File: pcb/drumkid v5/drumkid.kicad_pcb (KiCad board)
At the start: 2 copper layers, 51 parts, among them J1 Conn_01x02_Female, J5 Conn_01x05_Female, J6 Conn_01x04_Female, J7 Conn_01x06_Female, J8 Conn_01x05_Female, J9 AudioJack3_Ground_Switch, SW1 SW_SPDT, SW2 SW_Push, SW3 SW_Push, SW4 SW_Push, SW5 SW_Push, SW6 SW_Push, SW7 SW_Push, U2 ATmega328P-PU, U3 LM386, Y1 Crystal

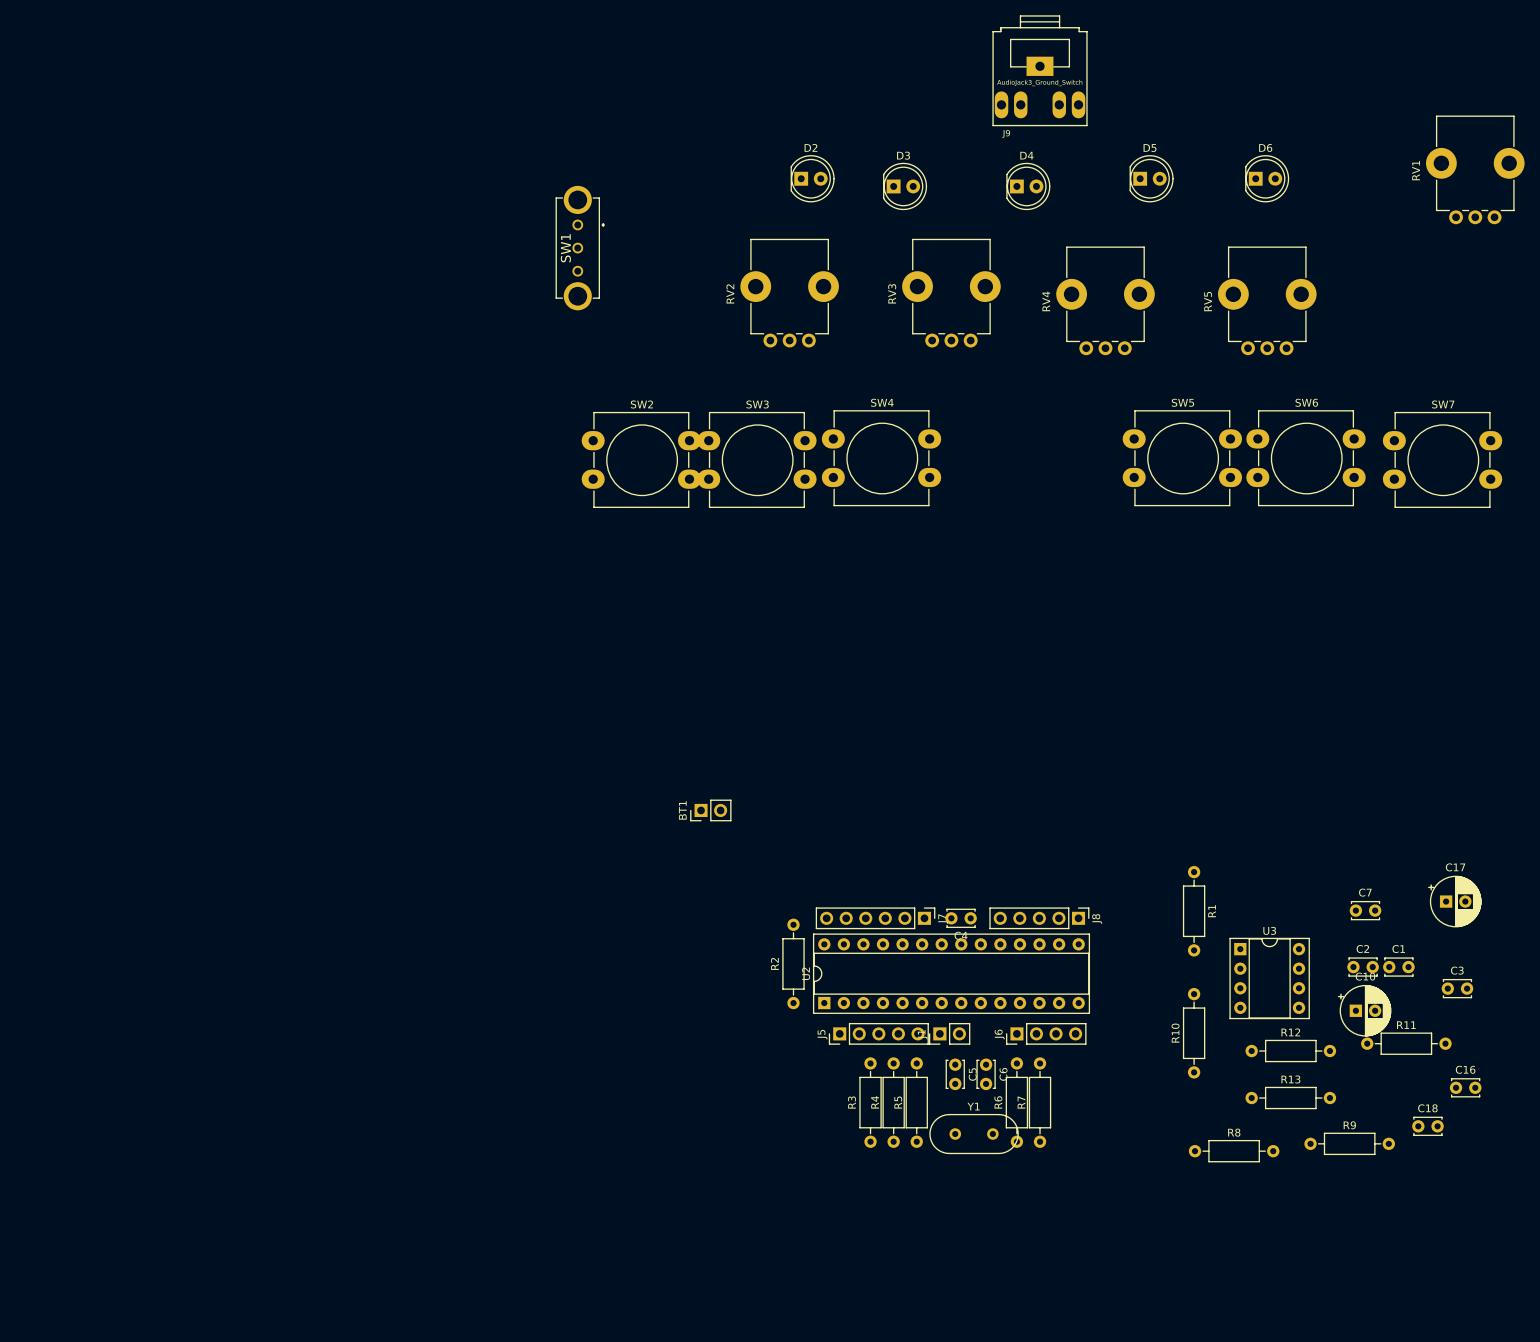
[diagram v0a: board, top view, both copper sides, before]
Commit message: lots of new stuff - pcb v5 progress, midi code progress, but lots to be done
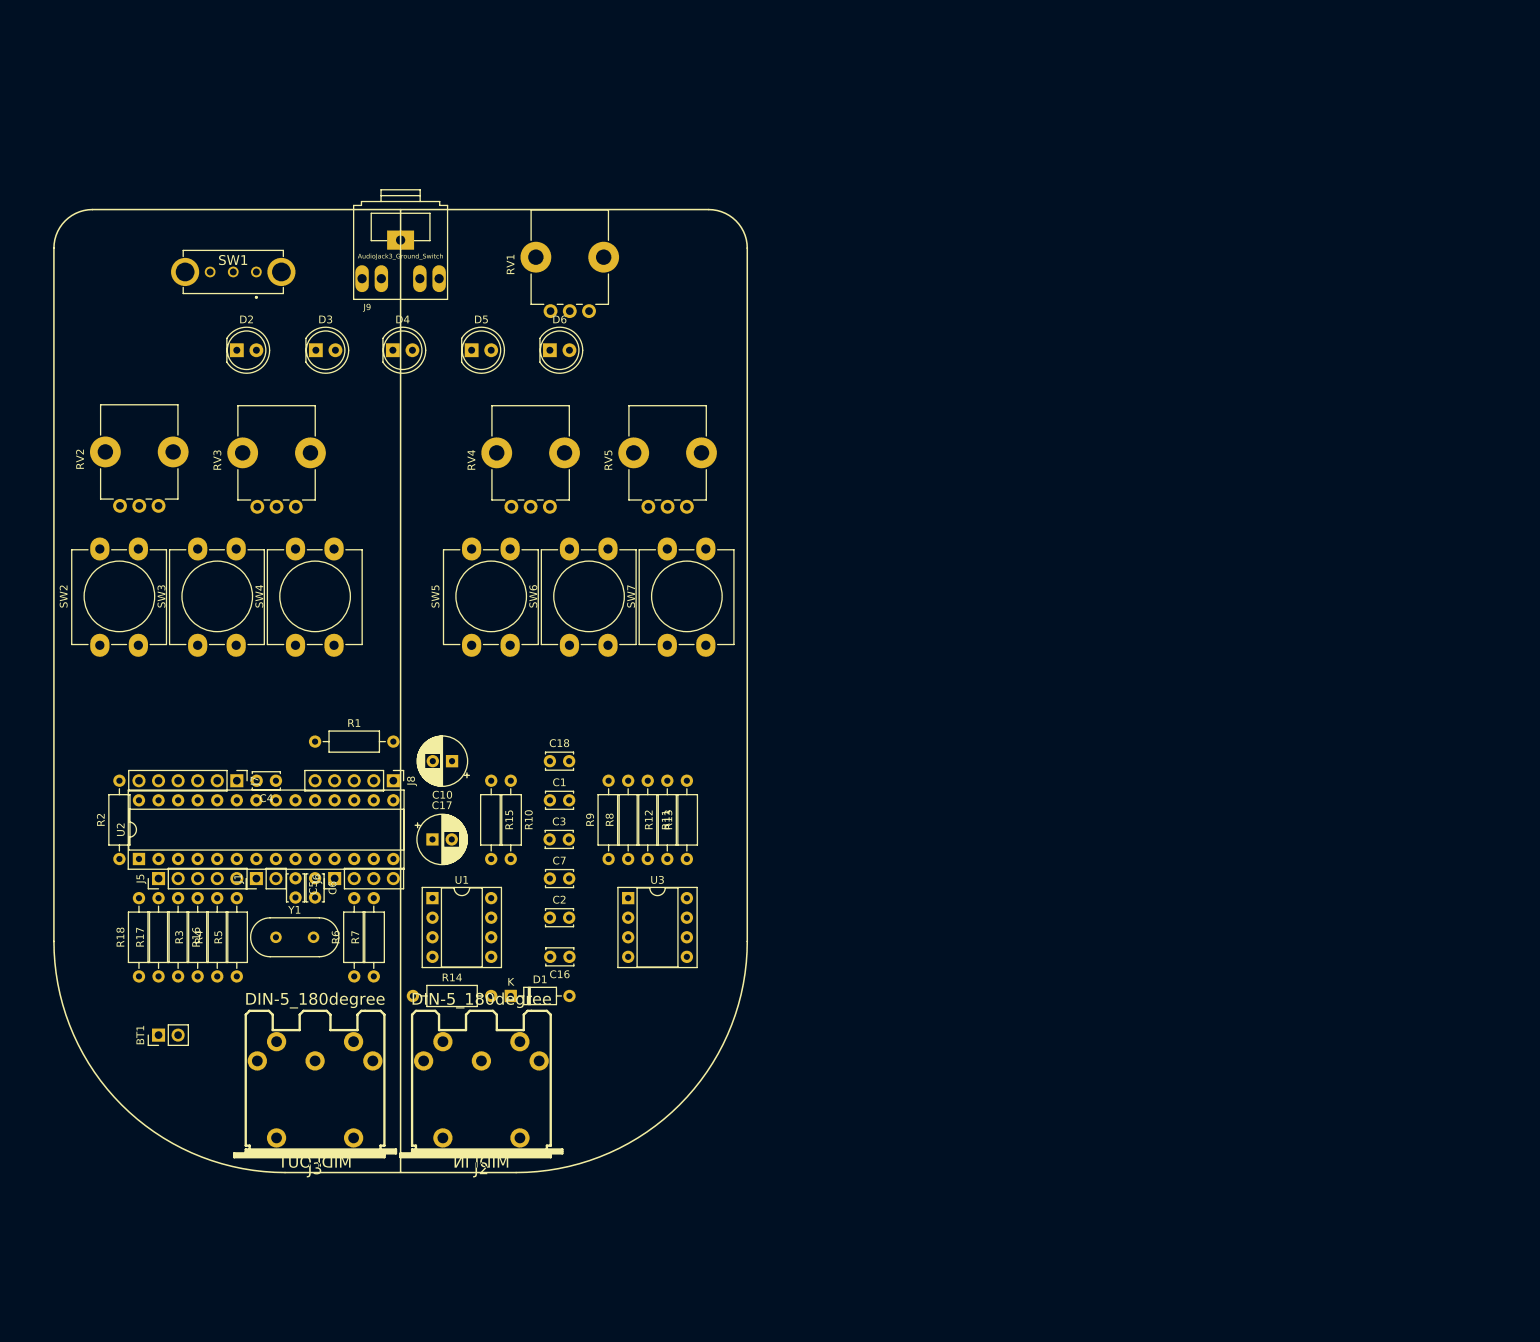
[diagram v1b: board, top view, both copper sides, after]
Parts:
- added D1: 1N4148, Diode_THT:D_DO-35_SOD27_P7.62mm_Horizontal, F.Cu at (114.3, 132.1)
- added J2: DIN-5_180degree, Eurocad:MIDI_DIN5, F.Cu at (110.5, 143.5)
- added J3: DIN-5_180degree, Eurocad:MIDI_DIN5, F.Cu at (88.9, 143.5)
- added R14: 220, Resistor_THT:R_Axial_DIN0207_L6.3mm_D2.5mm_P10.16mm_Horizontal, F.Cu at (101.6, 132.1)
- added R15: 10k, Resistor_THT:R_Axial_DIN0207_L6.3mm_D2.5mm_P10.16mm_Horizontal, F.Cu at (111.8, 104.1)
- added R16: 220, Resistor_THT:R_Axial_DIN0207_L6.3mm_D2.5mm_P10.16mm_Horizontal, F.Cu at (71.1, 119.4)
- added R17: 470, Resistor_THT:R_Axial_DIN0207_L6.3mm_D2.5mm_P10.16mm_Horizontal, F.Cu at (68.6, 129.5)
- added R18: 220, Resistor_THT:R_Axial_DIN0207_L6.3mm_D2.5mm_P10.16mm_Horizontal, F.Cu at (66.0, 129.5)
- added U1: 6N138, Package_DIP:DIP-8_W7.62mm_Socket, F.Cu at (104.1, 119.4)
- moved C17 131.8 mm to (104.1, 111.8)
- moved C18 122.3 mm to (119.4, 101.6)
- moved C10 121.7 mm to (106.7, 101.6), turned to 180 degrees
- moved C3 118.2 mm to (119.3, 111.8)
- moved RV1 118.2 mm to (124.5, 43.2)
- moved C16 116.3 mm to (121.9, 127.0), turned to 180 degrees
- moved R1 115.4 mm to (88.9, 99.1), turned to 0 degrees
- moved C1 111.1 mm to (119.4, 106.7)
- moved C7 104.7 mm to (119.4, 116.8)
- moved C2 104.5 mm to (119.4, 121.9)
- moved R11 99.4 mm to (132.1, 104.1), turned to 270 degrees
- moved R9 98.3 mm to (127.0, 114.3), turned to 90 degrees
- moved SW7 98.0 mm to (134.6, 86.6), turned to 90 degrees
- moved R10 96.4 mm to (114.3, 104.1), turned to 270 degrees
- moved D6 94.3 mm to (119.4, 48.3)
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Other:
- board text added: "MIDI IN"
- board text added: "MIDI OUT"

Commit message: more pcb progress
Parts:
- added D7: LED, LED_THT:LED_D5.0mm, B.Cu at (69.0, 50.0)
- added R19: 220, Resistor_THT:R_Axial_DIN0207_L6.3mm_D2.5mm_P10.16mm_Horizontal, F.Cu at (61.0, 104.1)
- BT1: footprint Connector_PinHeader_2.54mm:PinHeader_1x02_P2.54mm_Vertical -> Connector_Wire:SolderWirePad_1x02_P5.08mm_Drill1.5mm
- D2, D3, D4, D5, D6, J9, RV1, RV2, RV3, RV4, RV5, SW1, SW2, SW3, SW4, SW5, SW6, SW7: moved to B.Cu
- moved BT1 38.2 mm to (66.0, 99.1), turned to 0 degrees
- moved R14 33.1 mm to (134.6, 129.5), turned to 180 degrees
- moved R7 20.5 mm to (116.8, 127.0), turned to 180 degrees
- moved D1 13.7 mm to (127.0, 127.0)
- moved R6 10.5 mm to (104.1, 127.0), turned to 180 degrees
- moved D4 10.2 mm to (109.0, 50.0)
- moved D5 9.93 mm to (119.0, 50.0)
- moved D6 9.78 mm to (129.0, 50.0)
- moved SW2 7.82 mm to (61.0, 78.7), turned to 270 degrees
- moved SW3 7.82 mm to (73.7, 78.7), turned to 270 degrees
- moved SW4 7.82 mm to (86.4, 78.7), turned to 270 degrees
- moved SW5 7.82 mm to (109.2, 78.7), turned to 270 degrees
- moved SW6 7.82 mm to (121.9, 78.7), turned to 270 degrees
- moved SW7 7.82 mm to (134.6, 78.7), turned to 270 degrees
- moved RV3 5.12 mm to (81.3, 68.6)
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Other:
- board text added: "chance/pitch slop/beat drop"
- board text added: "midpoint/glitch delay_mix/drift drone pitch"
- board text added: "off"
- board text added: "on"
- board text added: "range/crop delay/time_sig drone mix"
- board text added: "zoom/crush swing/tempo drone_mod"

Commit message: more pcb stuff
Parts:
- added H1: MountingHole, MountingHole:MountingHole_3.2mm_M3, F.Cu at (60.0, 35.0)
- added H2: MountingHole, MountingHole:MountingHole_3.2mm_M3, F.Cu at (60.0, 110.0)
- added H3: MountingHole, MountingHole:MountingHole_3.2mm_M3, F.Cu at (70.0, 160.0)
- added H4: MountingHole, MountingHole:MountingHole_3.2mm_M3, F.Cu at (130.0, 160.0)
- added H5: MountingHole, MountingHole:MountingHole_3.2mm_M3, F.Cu at (140.0, 110.0)
- added H6: MountingHole, MountingHole:MountingHole_3.2mm_M3, F.Cu at (140.0, 35.0)
- moved R10 33.0 mm to (114.3, 132.1)
- moved R15 33.0 mm to (111.8, 132.1)
- moved R7 27.5 mm to (94.0, 142.2), turned to 90 degrees
- moved U1 20.9 mm to (99.1, 134.6)
- moved R6 19.8 mm to (91.4, 142.2), turned to 90 degrees
- moved J2 17.8 mm to (111.8, 157.5)
- moved J3 17.8 mm to (88.9, 157.5)
- moved C17 16.1 mm to (111.8, 124.5)
- moved Y1 15.2 mm to (83.8, 139.7), turned to 90 degrees
- moved C10 13.7 mm to (111.8, 114.3)
- moved R16 13.0 mm to (71.1, 132.1)
- moved R18 13.0 mm to (66.0, 142.2)
- moved R4 13.0 mm to (76.2, 142.2)
- moved R17 13.0 mm to (68.6, 142.2)
- moved R3 13.0 mm to (73.7, 142.2)
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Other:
- board text added: "A"
- board text added: "B"
- board text added: "C"
- board text added: "SERIAL NUMBER"
- board text added: "X"
- board text added: "Y"
- board text added: "Z"
- board text removed: "chance/pitch slop/beat drop"
- board text removed: "midpoint/glitch delay_mix/drift drone pitch"
- board text removed: "range/crop delay/time_sig drone mix"
- board text removed: "zoom/crush swing/tempo drone_mod"

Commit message: and more pcb stuff
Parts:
- added H7: MountingHole, MountingHole:MountingHole_3.2mm_M3, F.Cu at (100.0, 50.0)
- added H8: MountingHole, MountingHole:MountingHole_3.2mm_M3, F.Cu at (100.0, 80.0)
- moved RV1 12.0 mm to (115.0, 44.0)
- moved R1 8.03 mm to (81.3, 106.7)
- moved SW1 3.38 mm to (79.0, 40.0)
- moved RV3 2.54 mm to (78.7, 68.6)
- moved RV4 2.54 mm to (116.8, 68.6)
- moved BT1 2.54 mm to (71.1, 106.7)
- moved J9 1.44 mm to (100.0, 37.0)
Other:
- board outline added: 90 x 140 mm
- board text added: "0"
- board text added: "1"
- board text added: "8 7 6 5 GND VCC 4 3 2 1 0"
- board text added: "9 10 11 12 13 A0 A1 A2 A3 A4 A5"
- board text added: "d"
- board text added: "k"
- board text removed: "off"
- board text removed: "on"

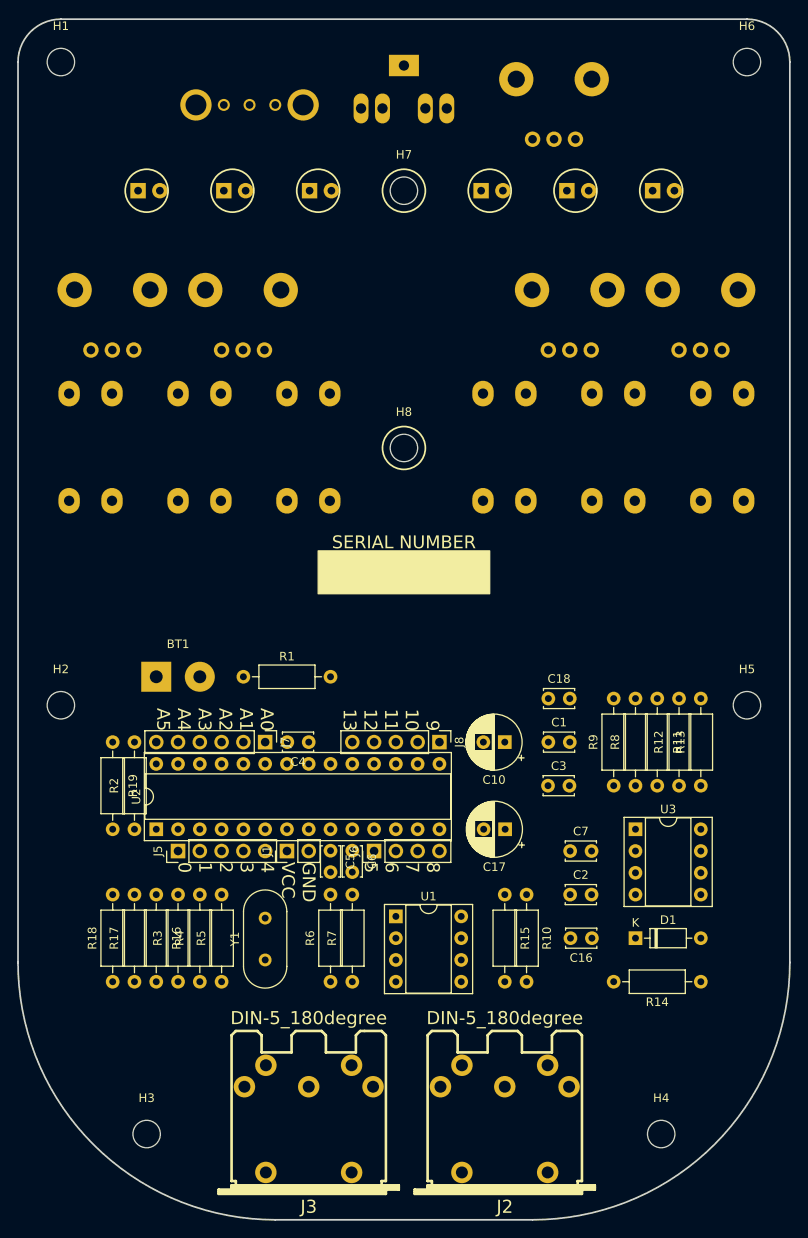
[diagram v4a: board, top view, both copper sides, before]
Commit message: finished messing about with pcb layout, next comes routing...
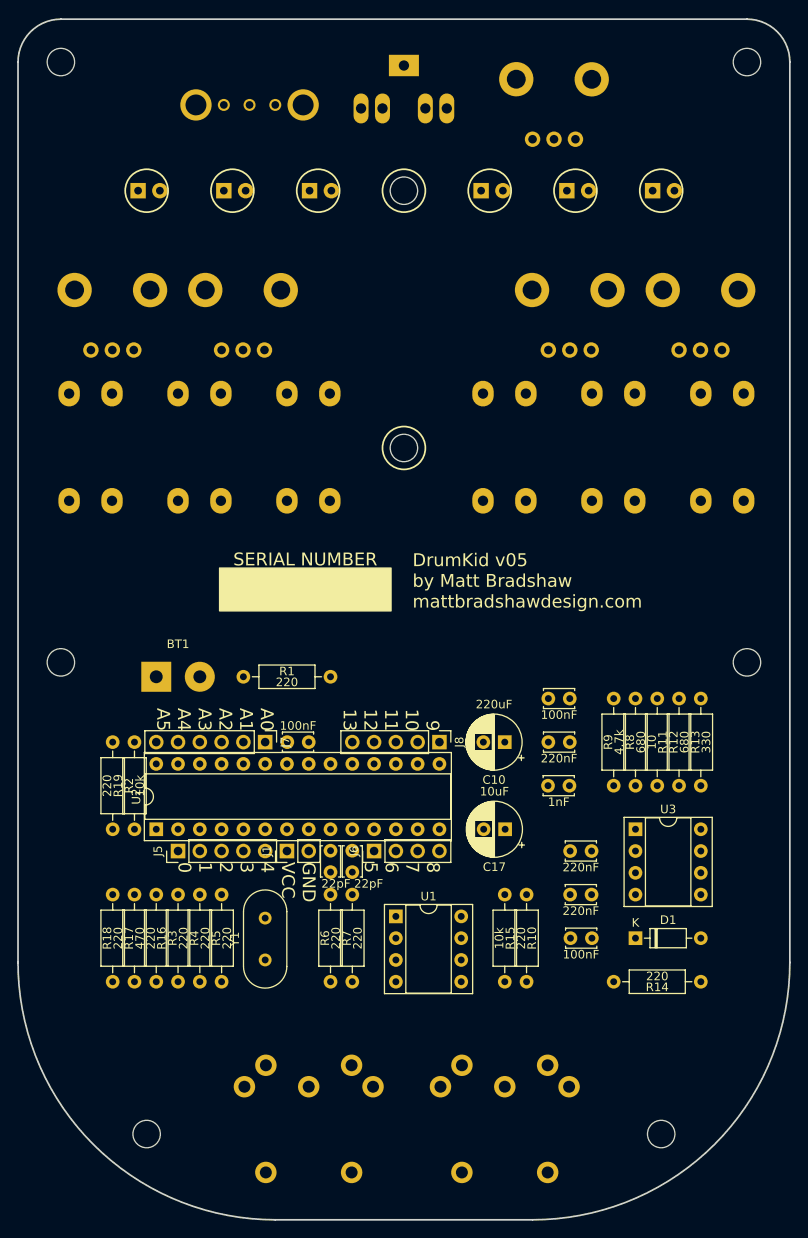
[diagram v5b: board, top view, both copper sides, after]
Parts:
- C1, C16, C18, C2, C3, C4, C5, C6, C7: footprint Capacitor_THT:C_Disc_D3.4mm_W2.1mm_P2.50mm -> drumkidcustom:C_Disc_D3.4mm_W2.1mm_P2.50mm
- C10, C17: footprint Capacitor_THT:CP_Radial_D6.3mm_P2.50mm -> drumkidcustom:CP_Radial_D6.3mm_P2.50mm
- D2, D3, D4, D5, D6, D7: footprint LED_THT:LED_D5.0mm -> drumkidcustom:LED_D5.0mm
- H1, H2, H3, H4, H5, H6, H7, H8: footprint MountingHole:MountingHole_3.2mm_M3 -> drumkidcustom:MountingHole_3.2mm_M3
- J2, J3: footprint Eurocad:MIDI_DIN5 -> drumkidcustom:MIDI_DIN5
- J9: footprint headphone:Tayda_3.5mm_stereo_TRS_jack_A-853 -> drumkidcustom:Tayda_3.5mm_stereo_TRS_jack_A-853
- R1, R10, R11, R12, R13, R14, R15, R16, R17, R18, R19, R2, R3, R4, R5, R6, R7, R8, R9: footprint Resistor_THT:R_Axial_DIN0207_L6.3mm_D2.5mm_P10.16mm_Horizontal -> drumkidcustom:R_Axial_DIN0207_L6.3mm_D2.5mm_P10.16mm_Horizontal
- SW1: footprint SamacSys_Parts:EG1206 -> drumkidcustom:EG1206
- SW2, SW3, SW4, SW5, SW6, SW7: footprint Button_Switch_THT:SW_PUSH-12mm_Wuerth-430476085716 -> drumkidcustom:SW_PUSH-12mm_Wuerth-430476085716
- moved H2 5.00 mm to (60.0, 105.0)
- moved H5 5.00 mm to (140.0, 105.0)
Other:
- board text added: "DrumKid v05 by Matt Bradshaw mattbradshawdesign.com"

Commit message: routing done except for gnd
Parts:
- moved RV2 68.6 mm to (132.1, 68.6)
- moved RV5 68.6 mm to (63.5, 68.6)
- moved RV3 38.1 mm to (116.8, 68.6)
- moved RV4 38.1 mm to (78.7, 68.6)
- moved Y1 5.24 mm to (85.1, 134.6), turned to 270 degrees
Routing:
- net +5V: track 0.00 -> 295.7 mm
- net Net-(D4-Pad2): track 0.00 -> 184.2 mm
- net Net-(D5-Pad2): track 0.00 -> 162.1 mm
- net Net-(D3-Pad2): track 0.00 -> 139.0 mm
- net Net-(D6-Pad2): track 0.00 -> 136.2 mm
- net /ANALOG_1: track 0.00 -> 129.2 mm
- net Net-(D2-Pad2): track 0.00 -> 114.7 mm
- net Net-(C7-Pad1): track 0.00 -> 110.1 mm
- net /ANALOG_0: track 0.00 -> 94.7 mm
- net Net-(BT1-Pad1): track 0.00 -> 92.1 mm
- net Net-(C10-Pad2): track 0.00 -> 88.4 mm
- net /DIGITAL_7: track 0.00 -> 86.5 mm, vias 0 -> 2
- net /DIGITAL_13: track 0.00 -> 82.1 mm
- net Net-(R9-Pad2): track 0.00 -> 81.2 mm
- net GND: track 0.00 -> 75.0 mm
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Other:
- net class Chunky added: clearance 0.2, trace_width 0.625, via_dia 0.8, via_drill 0.4

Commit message: routing done
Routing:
- net GND: track 75.0 -> 268.4 mm, vias 0 -> 4
- net Net-(C3-Pad1): track 0.00 -> 31.8 mm, vias 0 -> 1
- net Net-(R10-Pad1): track 14.8 -> 32.9 mm, vias 0 -> 1
- net Net-(C18-Pad2): track 0.00 -> 14.0 mm
- net /ANALOG_0: track 94.7 -> 99.0 mm
- net Net-(C1-Pad1): track 73.9 -> 76.0 mm
- net /ANALOG_1: track 129.2 -> 127.4 mm
- added copper zone on B.Cu, net GND
- added copper zone on F.Cu, net GND
